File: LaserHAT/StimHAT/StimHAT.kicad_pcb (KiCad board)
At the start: 4 copper layers, 65 x 57 mm, 113 parts, among them J1 GPIO, J10 OLED 0.91 (GND VCC SCL SDA), J101 ELECTRODE E1/E2, J102 B4B-PH-K-S(LF)(SN), J103 5V TO DC-DC POD, J5 GT-USB-7010ASV, J6 BNC TRIGGER IN, J7 BNC STIM OUT, Q3 AP30P30Q, Q4 DMMT5401, Q5 AP30P30Q, SW10 MSK12C02, SW6 TS-1088-AR02016, SW7 SKRHADE010, SW9 TS-1088-AR02016, U1 M24C32-WDW6TP, U101 ISO7741FDBQR, U104 TLV76050DBZR, U105 DAC60501ZDGSR, U106 OPA2192IDGKR, U107 CD74HC4053PWR, U108 DG418DY-T1-E3, U109 ISO1640BDR, U110 TLV1702AIDGKR, U4 MCP1700T-3302E/MB, U5 AP2171W, U6 CH340N, U7 MSPM0G1507SRHBR, U8 74LVC2G17GW

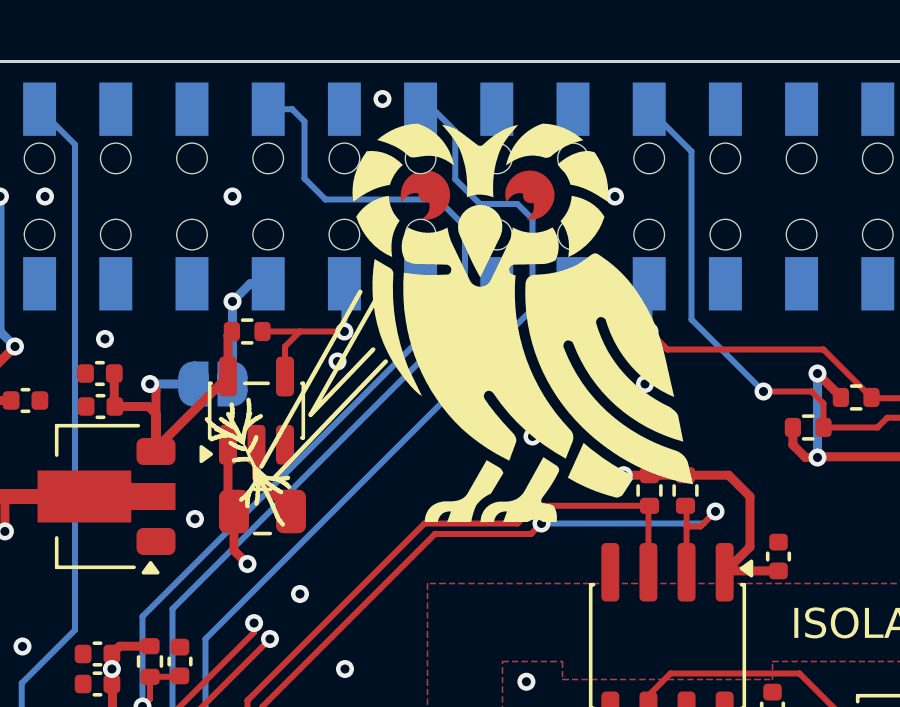
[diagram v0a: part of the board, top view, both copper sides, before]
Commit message: StimHAT: owl mirrored to look right
tools/owl_logo.py gains MIRROR (x negated for every point, sizes untouched) and writes
stimhat:OwlLogo_Eyes_14mm_R; G1 stays at the user's (34.75, 8.75) by the Pi header.  As
committed the eyes at y 4.4 hit J1's pass-through holes (3 hole-clearance errors) until the
user shifts the owl down.  Placement table synced (C2 / R7 / U5 / JP5 / G1).

Co-Authored-By: Claude Fable 5.1 <noreply@anthropic.com>
Claude-Session: https://claude.ai/code/session_015kiXLxnPpBaXdXJu2EMvn7
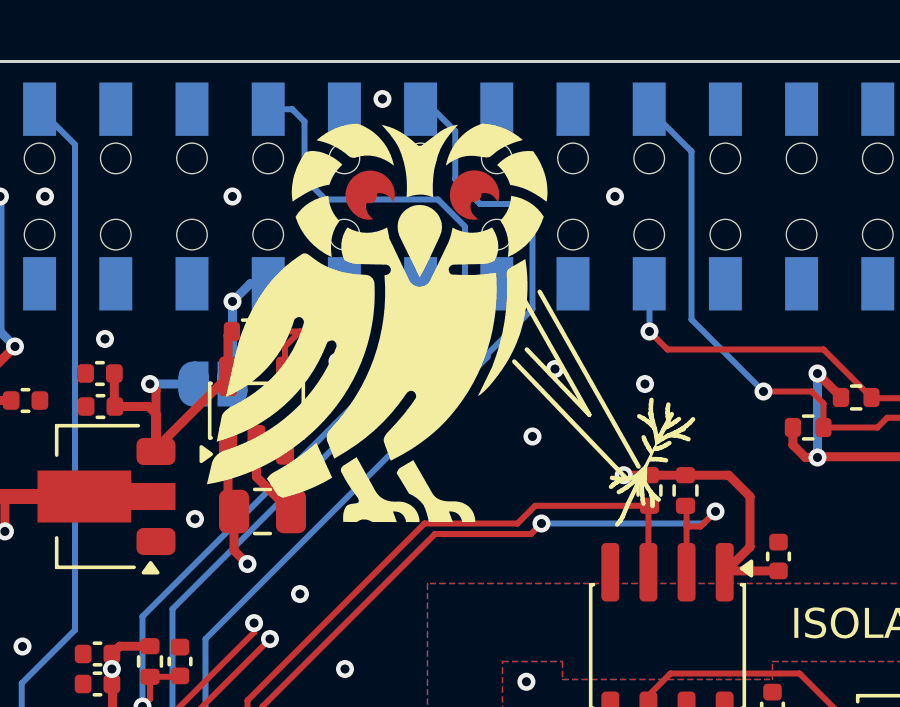
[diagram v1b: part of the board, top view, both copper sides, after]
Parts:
- G1: value OwlLogo_Eyes_14mm -> OwlLogo_Eyes_14mm_R; footprint stimhat:OwlLogo_Eyes_14mm -> stimhat:OwlLogo_Eyes_14mm_R
